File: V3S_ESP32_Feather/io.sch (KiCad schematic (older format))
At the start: 18 parts, among them J3 CAM, J7 Micro_SD_Card_Det, U1 V3S, Y1 X1E0000210832, Y2 CC5V-T1A 32.768KHZ +-20PPM 12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

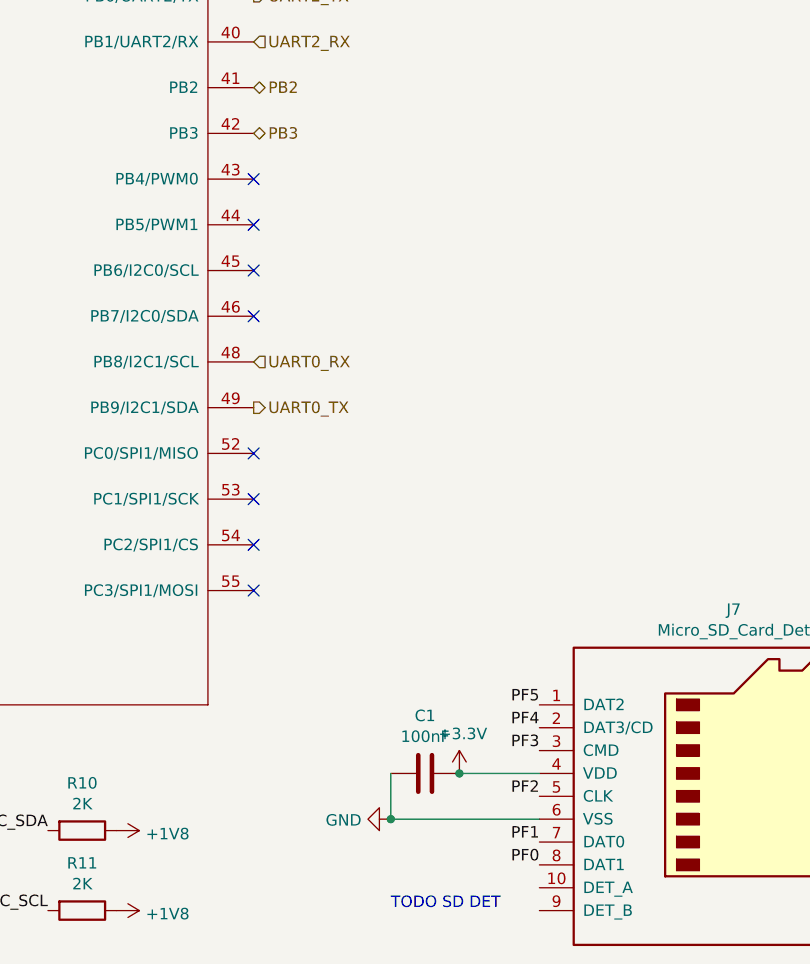
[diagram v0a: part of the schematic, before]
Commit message: Add i2c connector from V3s, fix sd card detection and remove todos
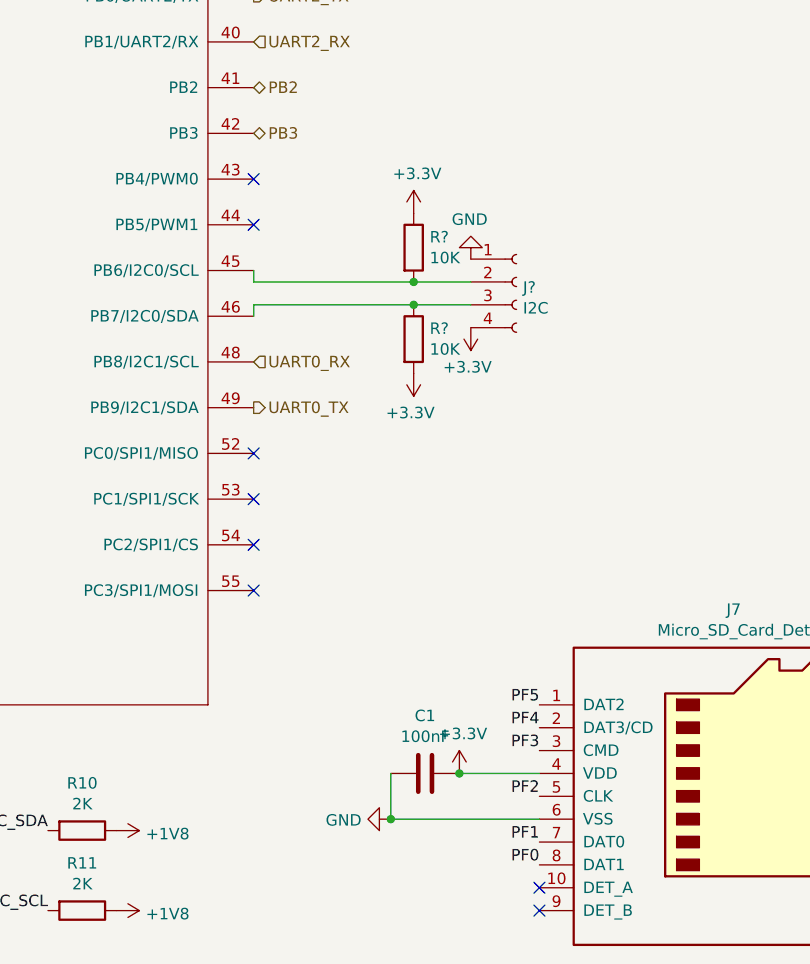
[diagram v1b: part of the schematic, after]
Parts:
- added J?: I2C, symbol Connector:Conn_01x04_Female
- added R? (x2): 10K, symbol Device:R
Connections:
- net +3V3: now also J?.4 (Pin_4), R?.1, R?.2
- net GND: now also J?.1 (Pin_1)
- net at U1.45 (PB6/I2C0/SCL): now also J?.2 (Pin_2), R?.2
- net at U1.46 (PB7/I2C0/SDA): now also J?.3 (Pin_3), R?.1
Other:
- note removed: "TODO SD DET"
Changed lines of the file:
@@
 	1    0    0    -1
 $EndComp
-Text Notes 4100 7350 0    50   ~ 0
-TODO SD DET
 $Comp
 L Device:C C1
@@
 NoConn ~ 3500 5550
 NoConn ~ 3500 5950
-NoConn ~ 3500 4550
-NoConn ~ 3500 4750
 Text HLabel 3950 3150 2    50   BiDi ~ 0
 USB_ID
@@
 Wire Wire Line
 	3950 3150 3500 3150
+$Comp
+L Connector:Conn_01x04_Female J?
+U 1 1 5D8935F1
+P 4650 4600
+F 0 "J?" H 4678 4576 50  0000 L CNN
+F 1 "I2C" H 4678 4485 50  0000 L CNN
+F 2 "" H 4650 4600 50  0001 C CNN
+F 3 "~" H 4650 4600 50  0001 C CNN
+	1    4650 4600
+	1    0    0    -1
+$EndComp
+Wire Wire Line
+	3500 4550 3500 4600
+Wire Wire Line
+	4450 4700 4200 4700
+Wire Wire Line
+	3500 4700 3500 4750
+$Comp
+L Device:R R?
+U 1 1 5D898760
+P 4200 4450
+F 0 "R?" H 4270 4496 50  0000 L CNN
+F 1 "10K" H 4270 4405 50  0000 L CNN
+F 2 "" V 4130 4450 50  0001 C CNN
+F 3 "~" H 4200 4450 50  0001 C CNN
+	1    4200 4450
+	1    0    0    -1
+$EndComp
+Connection ~ 4200 4600
+Wire Wire Line
+	4200 4600 4450 4600
+$Comp
+L Device:R R?
+U 1 1 5D89986A
+P 4200 4850
+F 0 "R?" H 4270 4896 50  0000 L CNN
+F 1 "10K" H 4270 4805 50  0000 L CNN
+F 2 "" V 4130 4850 50  0001 C CNN
+F 3 "~" H 4200 4850 50  0001 C CNN
+	1    4200 4850
+	1    0    0    -1
+$EndComp
+Connection ~ 4200 4700
+Wire Wire Line
+	3500 4600 4200 4600
+Wire Wire Line
+	3500 4700 4200 4700
+$Comp
+L power:+3.3V #PWR?
+U 1 1 5D89EBFE
+P 4200 4300
+F 0 "#PWR?" H 4200 4150 50  0001 C CNN
+F 1 "+3.3V" H 4215 4473 50  0000 C CNN
+F 2 "" H 4200 4300 50  0001 C CNN
+F 3 "" H 4200 4300 50  0001 C CNN
+	1    4200 4300
+	1    0    0    -1
+$EndComp
+$Comp
+L power:+3.3V #PWR?
+U 1 1 5D8A0291
+P 4200 5000
+F 0 "#PWR?" H 4200 4850 50  0001 C CNN
+F 1 "+3.3V" H 4215 5173 50  0000 C CNN
+F 2 "" H 4200 5000 50  0001 C CNN
+F 3 "" H 4200 5000 50  0001 C CNN
+	1    4200 5000
+	-1   0    0    1
+$EndComp
+$Comp
+L power:GND #PWR?
+U 1 1 5D8A2122
+P 4450 4500
+F 0 "#PWR?" H 4450 4250 50  0001 C CNN
+F 1 "GND" H 4455 4327 50  0000 C CNN
+F 2 "" H 4450 4500 50  0001 C CNN
+F 3 "" H 4450 4500 50  0001 C CNN
+	1    4450 4500
+	-1   0    0    1
+$EndComp
+$Comp
+L power:+3.3V #PWR?
+U 1 1 5D8A2EB4
+P 4450 4800
+F 0 "#PWR?" H 4450 4650 50  0001 C CNN
+F 1 "+3.3V" H 4465 4973 50  0000 C CNN
+F 2 "" H 4450 4800 50  0001 C CNN
+F 3 "" H 4450 4800 50  0001 C CNN
+	1    4450 4800
+	-1   0    0    1
+$EndComp
+NoConn ~ 4750 7250
+NoConn ~ 4750 7350
 $EndSCHEMATC

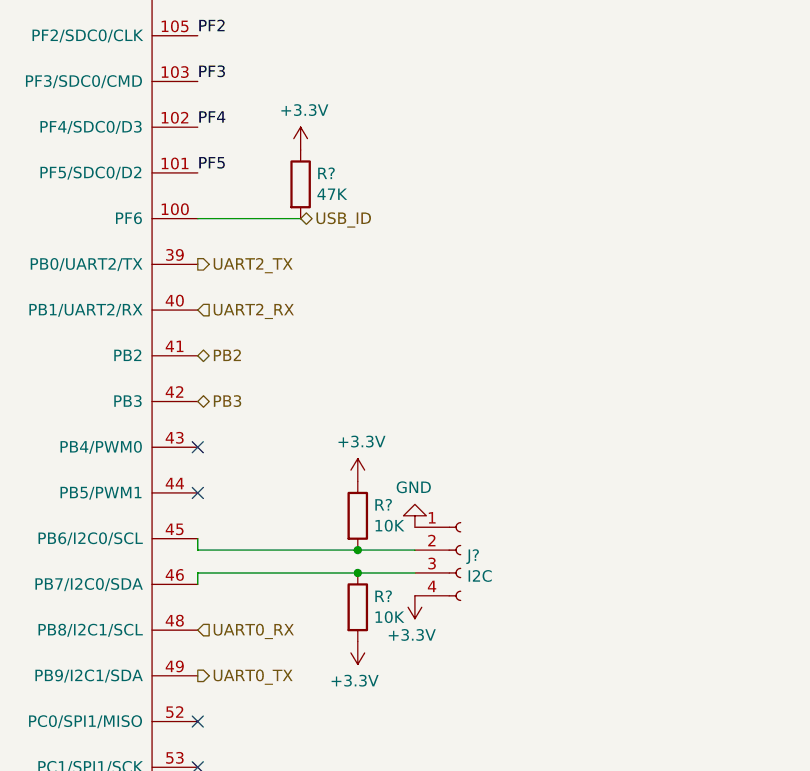
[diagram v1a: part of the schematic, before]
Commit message: Add more footprint, pcb format done, started component placement
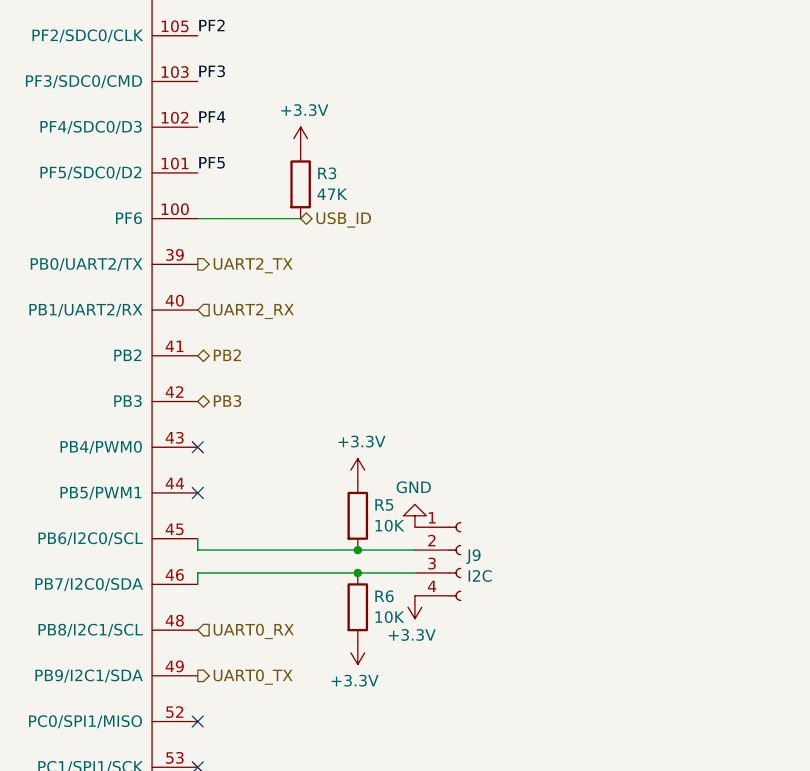
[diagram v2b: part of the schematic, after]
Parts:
- C1: footprint (none) -> Capacitor_SMD:C_0201_0603Metric
- J3: footprint (none) -> fpc_cam24:FPC_24_CAM
- J9: renamed from J?; footprint (none) -> Connector_PinSocket_1.00mm:PinSocket_1x04_P1.00mm_Vertical
- R3, R5, R6: renamed from R?; footprint (none) -> Resistor_SMD:R_0201_0603Metric
- RN1: footprint (none) -> Resistor_SMD:R_Array_Concave_4x0402
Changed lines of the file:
@@
 F 0 "J3" H 7978 1776 50  0000 L CNN
 F 1 "CAM" H 7978 1685 50  0000 L CNN
-F 2 "" H 7950 1800 50  0001 C CNN
+F 2 "fpc_cam24:FPC_24_CAM" H 7950 1800 50  0001 C CNN
 F 3 "~" H 7950 1800 50  0001 C CNN
 	1    7950 1800
@@
 F 0 "C1" V 3998 6750 50  0000 C CNN
 F 1 "100nF" V 4089 6750 50  0000 C CNN
-F 2 "" H 4288 6600 50  0001 C CNN
+F 2 "Capacitor_SMD:C_0201_0603Metric" H 4288 6600 50  0001 C CNN
 F 3 "~" H 4250 6750 50  0001 C CNN
 	1    4250 6750
@@
 F 0 "RN1" V 933 7350 50  0000 C CNN
 F 1 "47K" V 1024 7350 50  0000 C CNN
-F 2 "" V 1625 7350 50  0001 C CNN
+F 2 "Resistor_SMD:R_Array_Concave_4x0402" V 1625 7350 50  0001 C CNN
 F 3 "~" H 1350 7350 50  0001 C CNN
 	1    1350 7350
@@
 NoConn ~ 9150 1650
 $Comp
-L power:GND #PWR?
+L power:GND #PWR0163
 U 1 1 5D88B340
 P 9150 1050
-F 0 "#PWR?" H 9150 800 50  0001 C CNN
+F 0 "#PWR0163" H 9150 800 50  0001 C CNN
 F 1 "GND" H 9155 877 50  0000 C CNN
 F 2 "" H 9150 1050 50  0001 C CNN
@@
 USB_ID
 $Comp
-L Device:R R?
+L Device:R R3
 U 1 1 5D8D331F
 P 3950 3000
-F 0 "R?" H 4020 3046 50  0000 L CNN
+F 0 "R3" H 4020 3046 50  0000 L CNN
 F 1 "47K" H 4020 2955 50  0000 L CNN
-F 2 "" V 3880 3000 50  0001 C CNN
+F 2 "Resistor_SMD:R_0201_0603Metric" V 3880 3000 50  0001 C CNN
 F 3 "~" H 3950 3000 50  0001 C CNN
 	1    3950 3000
@@
 $EndComp
 $Comp
-L power:+3.3V #PWR?
+L power:+3.3V #PWR0164
 U 1 1 5D8D4966
 P 3950 2850
-F 0 "#PWR?" H 3950 2700 50  0001 C CNN
+F 0 "#PWR0164" H 3950 2700 50  0001 C CNN
 F 1 "+3.3V" H 3965 3023 50  0000 C CNN
 F 2 "" H 3950 2850 50  0001 C CNN
@@
 	3950 3150 3500 3150
 $Comp
-L Connector:Conn_01x04_Female J?
+L Connector:Conn_01x04_Female J9
 U 1 1 5D8935F1
 P 4650 4600
-F 0 "J?" H 4678 4576 50  0000 L CNN
+F 0 "J9" H 4678 4576 50  0000 L CNN
 F 1 "I2C" H 4678 4485 50  0000 L CNN
-F 2 "" H 4650 4600 50  0001 C CNN
+F 2 "Connector_PinSocket_1.00mm:PinSocket_1x04_P1.00mm_Vertical" H 4650 4600 50  0001 C CNN
 F 3 "~" H 4650 4600 50  0001 C CNN
 	1    4650 4600
@@
 	3500 4700 3500 4750
 $Comp
-L Device:R R?
+L Device:R R5
 U 1 1 5D898760
 P 4200 4450
-F 0 "R?" H 4270 4496 50  0000 L CNN
+F 0 "R5" H 4270 4496 50  0000 L CNN
 F 1 "10K" H 4270 4405 50  0000 L CNN
-F 2 "" V 4130 4450 50  0001 C CNN
+F 2 "Resistor_SMD:R_0201_0603Metric" V 4130 4450 50  0001 C CNN
 F 3 "~" H 4200 4450 50  0001 C CNN
 	1    4200 4450
@@
 	4200 4600 4450 4600
 $Comp
-L Device:R R?
+L Device:R R6
 U 1 1 5D89986A
 P 4200 4850
-F 0 "R?" H 4270 4896 50  0000 L CNN
+F 0 "R6" H 4270 4896 50  0000 L CNN
 F 1 "10K" H 4270 4805 50  0000 L CNN
-F 2 "" V 4130 4850 50  0001 C CNN
+F 2 "Resistor_SMD:R_0201_0603Metric" V 4130 4850 50  0001 C CNN
 F 3 "~" H 4200 4850 50  0001 C CNN
 	1    4200 4850
@@
 	3500 4700 4200 4700
 $Comp
-L power:+3.3V #PWR?
+L power:+3.3V #PWR0165
 U 1 1 5D89EBFE
 P 4200 4300
-F 0 "#PWR?" H 4200 4150 50  0001 C CNN
+F 0 "#PWR0165" H 4200 4150 50  0001 C CNN
 F 1 "+3.3V" H 4215 4473 50  0000 C CNN
 F 2 "" H 4200 4300 50  0001 C CNN
@@
 $EndComp
 $Comp
-L power:+3.3V #PWR?
+L power:+3.3V #PWR0171
 U 1 1 5D8A0291
 P 4200 5000
-F 0 "#PWR?" H 4200 4850 50  0001 C CNN
+F 0 "#PWR0171" H 4200 4850 50  0001 C CNN
 F 1 "+3.3V" H 4215 5173 50  0000 C CNN
 F 2 "" H 4200 5000 50  0001 C CNN
@@
 $EndComp
 $Comp
-L power:GND #PWR?
+L power:GND #PWR0172
 U 1 1 5D8A2122
 P 4450 4500
-F 0 "#PWR?" H 4450 4250 50  0001 C CNN
+F 0 "#PWR0172" H 4450 4250 50  0001 C CNN
 F 1 "GND" H 4455 4327 50  0000 C CNN
 F 2 "" H 4450 4500 50  0001 C CNN
@@
 $EndComp
 $Comp
-L power:+3.3V #PWR?
+L power:+3.3V #PWR0173
 U 1 1 5D8A2EB4
 P 4450 4800
-F 0 "#PWR?" H 4450 4650 50  0001 C CNN
+F 0 "#PWR0173" H 4450 4650 50  0001 C CNN
 F 1 "+3.3V" H 4465 4973 50  0000 C CNN
 F 2 "" H 4450 4800 50  0001 C CNN

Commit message: New component placement, progress on rooting
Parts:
- J9: footprint Connector_PinSocket_1.00mm:PinSocket_1x04_P1.00mm_Vertical -> Connector_JST:JST_SH_SM04B-SRSS-TB_1x04-1MP_P1.00mm_Horizontal
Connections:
- net PF0: now also RN1.1 (R1.1); no longer RN1.4 (R4.1)
- net PF1: now also RN1.2 (R2.1); no longer RN1.3 (R3.1)
- net PF3: now also RN1.3 (R3.1); no longer RN1.2 (R2.1)
- net PF4: now also RN1.4 (R4.1); no longer RN1.1 (R1.1)
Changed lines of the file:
@@
 Connection ~ 4400 6750
 NoConn ~ 3500 5750
-Text Label 1150 7250 2    50   ~ 0
+Text Label 1150 7350 2    50   ~ 0
 PF3
-Text Label 1150 7150 2    50   ~ 0
+Text Label 1150 7450 2    50   ~ 0
 PF4
 Text Label 1200 6850 2    50   ~ 0
 PF5
-Text Label 1150 7450 2    50   ~ 0
+Text Label 1150 7150 2    50   ~ 0
 PF0
-Text Label 1150 7350 2    50   ~ 0
+Text Label 1150 7250 2    50   ~ 0
 PF1
 $Comp
@@
 F 0 "J9" H 4678 4576 50  0000 L CNN
 F 1 "I2C" H 4678 4485 50  0000 L CNN
-F 2 "Connector_PinSocket_1.00mm:PinSocket_1x04_P1.00mm_Vertical" H 4650 4600 50  0001 C CNN
+F 2 "Connector_JST:JST_SH_SM04B-SRSS-TB_1x04-1MP_P1.00mm_Horizontal" H 4650 4600 50  0001 C CNN
 F 3 "~" H 4650 4600 50  0001 C CNN
 	1    4650 4600
